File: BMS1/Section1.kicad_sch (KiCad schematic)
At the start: 68 parts

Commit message: Cap Change
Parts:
- R79: footprint Resistor_SMD:R_2512_6332Metric_Pad1.40x3.35mm_HandSolder -> Resistor_SMD:R_0603_1608Metric_Pad0.98x0.95mm_HandSolder
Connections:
- net BatteryBus.C0: now also C39.2
- net BatteryBus.C1: now also C38.2
- net BatteryBus.C10: now also C29.2
- net BatteryBus.C11: now also C28.2
- net BatteryBus.C12: now also C27.2
- net BatteryBus.C2: now also C37.2
- net BatteryBus.C3: now also C36.2
- net BatteryBus.C4: now also C35.2
- net BatteryBus.C5: now also C34.2
- net BatteryBus.C6: now also C33.2
- net BatteryBus.C7: now also C32.1
- net BatteryBus.C8: now also C31.2, C32.2; no longer C32.1
- net BatteryBus.C9: now also C30.2
- net GND1: no longer C27.2, C28.2, C29.2, C30.2, C31.2, C32.2, C33.2, C34.2, C35.2, C36.2, C37.2, C38.2, C39.2
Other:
- moved on the sheet: C27, C28, C29, C30, C31, C32, C33, C34, C35, C36, C37, C38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

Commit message: Schematic (Self) Review Done
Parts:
- C27, C28, C29, C30, C31, C32, C33, C34, C35, C36, C37, C38, C39: value 100nF -> 15u
- R67, R68, R69, R70, R71, R72, R73, R74, R75, R76, R77, R78: value 21 -> 18
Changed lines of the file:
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@@
       (effects (font (size 1.27 1.27)) (justify right))
     )
-    (property "Value" "21" (at 84.582 184.15 90)
+    (property "Value" "18" (at 84.582 184.15 90)
       (effects (font (size 1.27 1.27)) (justify right))
     )
@@
       (effects (font (size 1.27 1.27)) (justify right))
     )
-    (property "Value" "21" (at 84.963 107.95 90)
+    (property "Value" "18" (at 84.963 107.95 90)
       (effects (font (size 1.27 1.27)) (justify right))
     )
@@
       (effects (font (size 1.27 1.27)) (justify right))
     )
-    (property "Value" "21" (at 85.471 168.783 90)
+    (property "Value" "18" (at 85.471 168.783 90)
       (effects (font (size 1.27 1.27)) (justify right))
     )
@@
       (effects (font (size 1.27 1.27)) (justify right))
     )
-    (property "Value" "21" (at 85.725 214.503 90)
+    (property "Value" "18" (at 85.725 214.503 90)
       (effects (font (size 1.27 1.27)) (justify right))
     )
@@
       (effects (font (size 1.27 1.27)))
     )
-    (property "Value" "100nF" (at 102.616 99.06 0)
+    (property "Value" "15u" (at 102.616 99.06 0)
       (effects (font (size 1.27 1.27)))
     )
@@
       (effects (font (size 1.27 1.27)) (justify right))
     )
-    (property "Value" "21" (at 84.963 123.317 90)
+    (property "Value" "18" (at 84.963 123.317 90)
       (effects (font (size 1.27 1.27)) (justify right))
     )
@@
       (effects (font (size 1.27 1.27)))
     )
-    (property "Value" "100nF" (at 102.87 128.778 0)
+    (property "Value" "15u" (at 102.87 128.778 0)
       (effects (font (size 1.27 1.27)))
     )
@@
       (effects (font (size 1.27 1.27)) (justify right))
     )
-    (property "Value" "21" (at 84.836 92.964 90)
+    (property "Value" "18" (at 84.836 92.964 90)
       (effects (font (size 1.27 1.27)) (justify right))
     )
@@
       (effects (font (size 1.27 1.27)))
     )
-    (property "Value" "100nF" (at 102.616 37.592 0)
+    (property "Value" "15u" (at 102.616 37.592 0)
       (effects (font (size 1.27 1.27)))
     )
@@
       (effects (font (size 1.27 1.27)))
     )
-    (property "Value" "100nF" (at 103.124 173.99 0)
+    (property "Value" "15u" (at 103.124 173.99 0)
       (effects (font (size 1.27 1.27)))
     )
@@
       (effects (font (size 1.27 1.27)))
     )
-    (property "Value" "100nF" (at 102.87 205.232 0)
+    (property "Value" "15u" (at 102.87 205.232 0)
       (effects (font (size 1.27 1.27)))
     )
@@
       (effects (font (size 1.27 1.27)) (justify right))
     )
-    (property "Value" "21" (at 85.217 153.416 90)
+    (property "Value" "18" (at 85.217 153.416 90)
       (effects (font (size 1.27 1.27)) (justify right))
     )
@@
       (effects (font (size 1.27 1.27)) (justify right))
     )
-    (property "Value" "21" (at 85.217 46.99 90)
+    (property "Value" "18" (at 85.217 46.99 90)
       (effects (font (size 1.27 1.27)) (justify right))
     )
@@
       (effects (font (size 1.27 1.27)) (justify right))
     )
-    (property "Value" "21" (at 84.963 199.39 90)
+    (property "Value" "18" (at 84.963 199.39 90)
       (effects (font (size 1.27 1.27)) (justify right))
     )
@@
       (effects (font (size 1.27 1.27)))
     )
-    (property "Value" "100nF" (at 103.632 144.78 0)
+    (property "Value" "15u" (at 103.632 144.78 0)
       (effects (font (size 1.27 1.27)))
     )
@@
       (effects (font (size 1.27 1.27)))
     )
-    (property "Value" "100nF" (at 102.616 221.107 0)
+    (property "Value" "15u" (at 102.616 221.107 0)
       (effects (font (size 1.27 1.27)))
     )
@@
       (effects (font (size 1.27 1.27)) (justify right))
     )
-    (property "Value" "21" (at 86.995 62.103 90)
+    (property "Value" "18" (at 86.995 62.103 90)
       (effects (font (size 1.27 1.27)) (justify right))
     )
@@
       (effects (font (size 1.27 1.27)))
     )
-    (property "Value" "100nF" (at 103.378 159.766 0)
+    (property "Value" "15u" (at 103.378 159.766 0)
       (effects (font (size 1.27 1.27)))
     )
@@
       (effects (font (size 1.27 1.27)))
     )
-    (property "Value" "100nF" (at 102.616 113.03 0)
+    (property "Value" "15u" (at 102.616 113.03 0)
       (effects (font (size 1.27 1.27)))
     )
@@
       (effects (font (size 1.27 1.27)))
     )
-    (property "Value" "100nF" (at 102.362 68.326 0)
+    (property "Value" "15u" (at 102.362 68.326 0)
       (effects (font (size 1.27 1.27)))
     )
@@
       (effects (font (size 1.27 1.27)))
     )
-    (property "Value" "100nF" (at 102.362 83.312 0)
+    (property "Value" "15u" (at 102.362 83.312 0)
       (effects (font (size 1.27 1.27)))
     )
@@
       (effects (font (size 1.27 1.27)))
     )
-    (property "Value" "100nF" (at 102.616 53.086 0)
+    (property "Value" "15u" (at 102.616 53.086 0)
       (effects (font (size 1.27 1.27)))
     )
@@
       (effects (font (size 1.27 1.27)))
     )
-    (property "Value" "100nF" (at 102.87 189.484 0)
+    (property "Value" "15u" (at 102.87 189.484 0)
       (effects (font (size 1.27 1.27)))
     )
@@
       (effects (font (size 1.27 1.27)) (justify right))
     )
-    (property "Value" "21" (at 84.328 138.43 90)
+    (property "Value" "18" (at 84.328 138.43 90)
       (effects (font (size 1.27 1.27)) (justify right))
     )
@@
       (effects (font (size 1.27 1.27)) (justify right))
     )
-    (property "Value" "21" (at 85.217 77.724 90)
-      (effects (font (size 1.27 1.27)) (justify right))
-    )
+    (property "Value" "18" (at 85.217 77.724 90)
+      (effects (font (size 1.27 1.27)) (justify right))
+    )

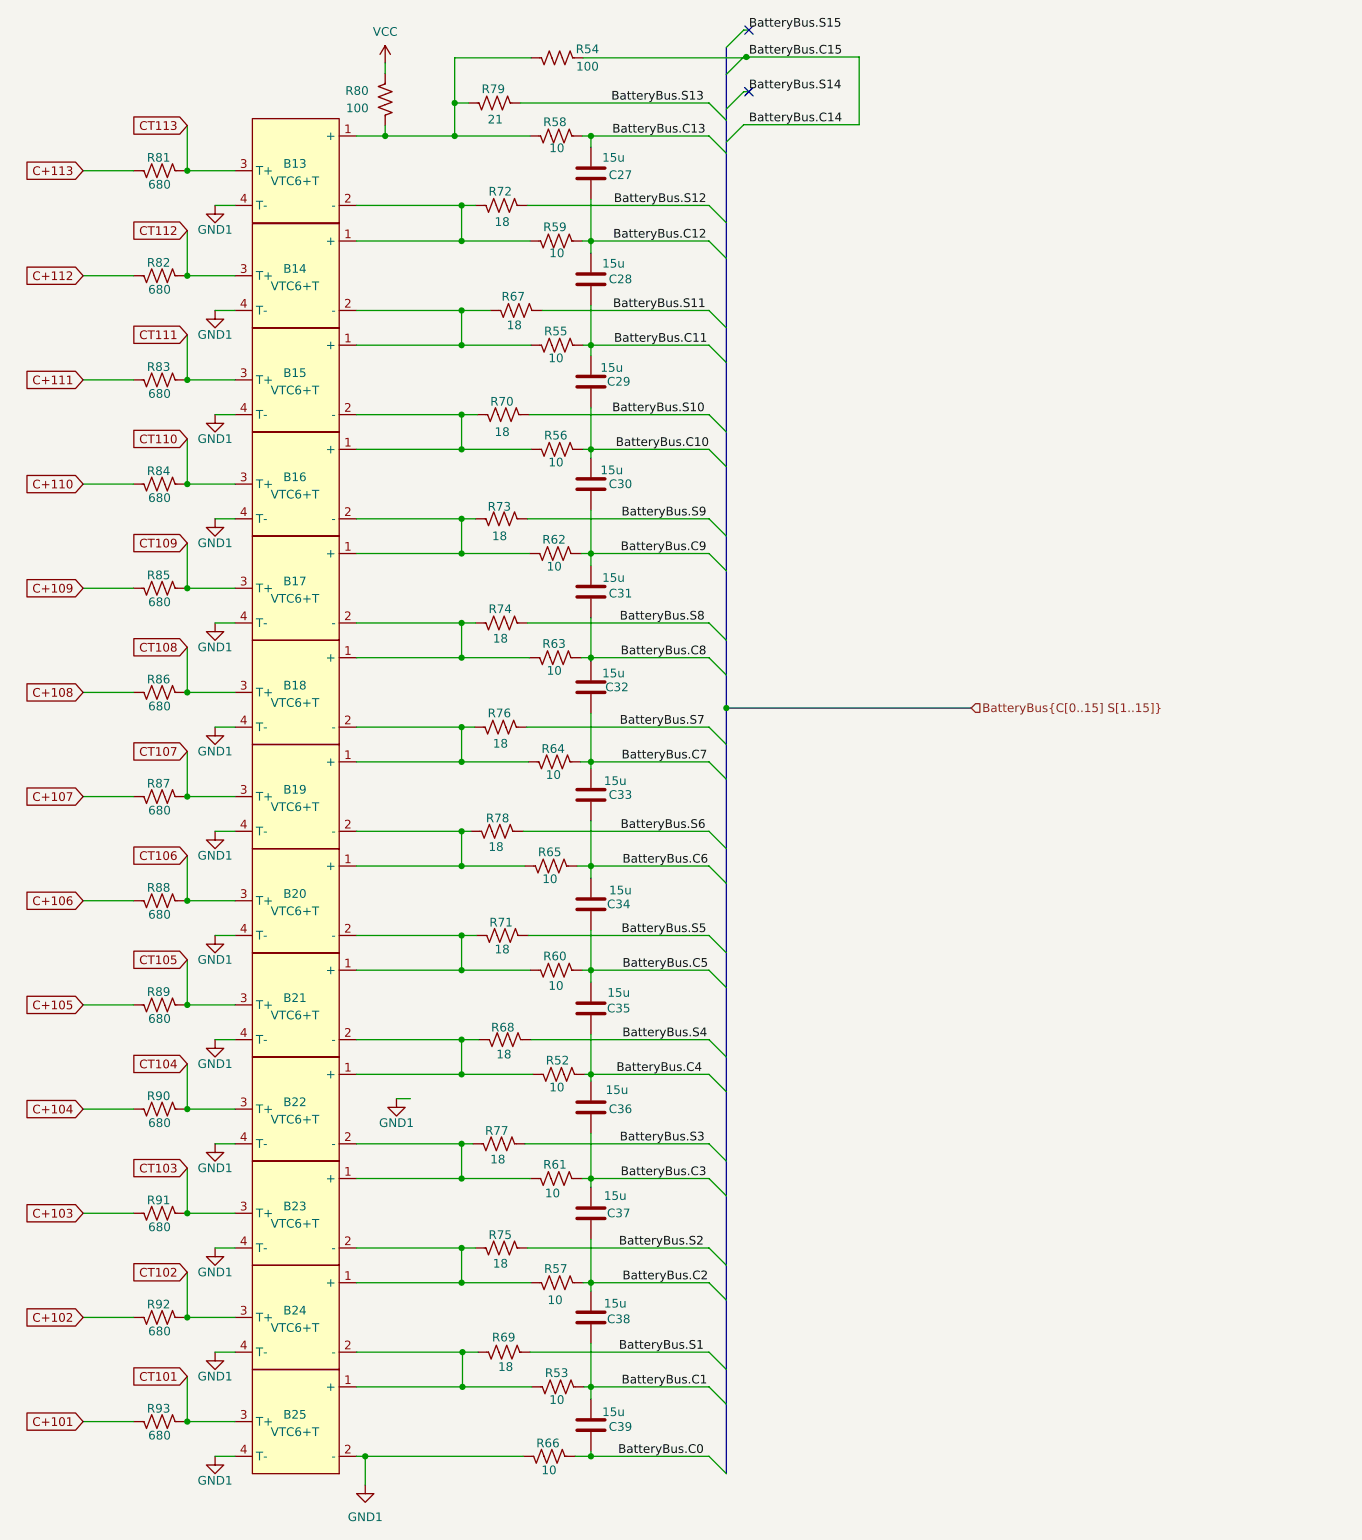
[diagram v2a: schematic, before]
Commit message: fixed to whats on board footy not changed
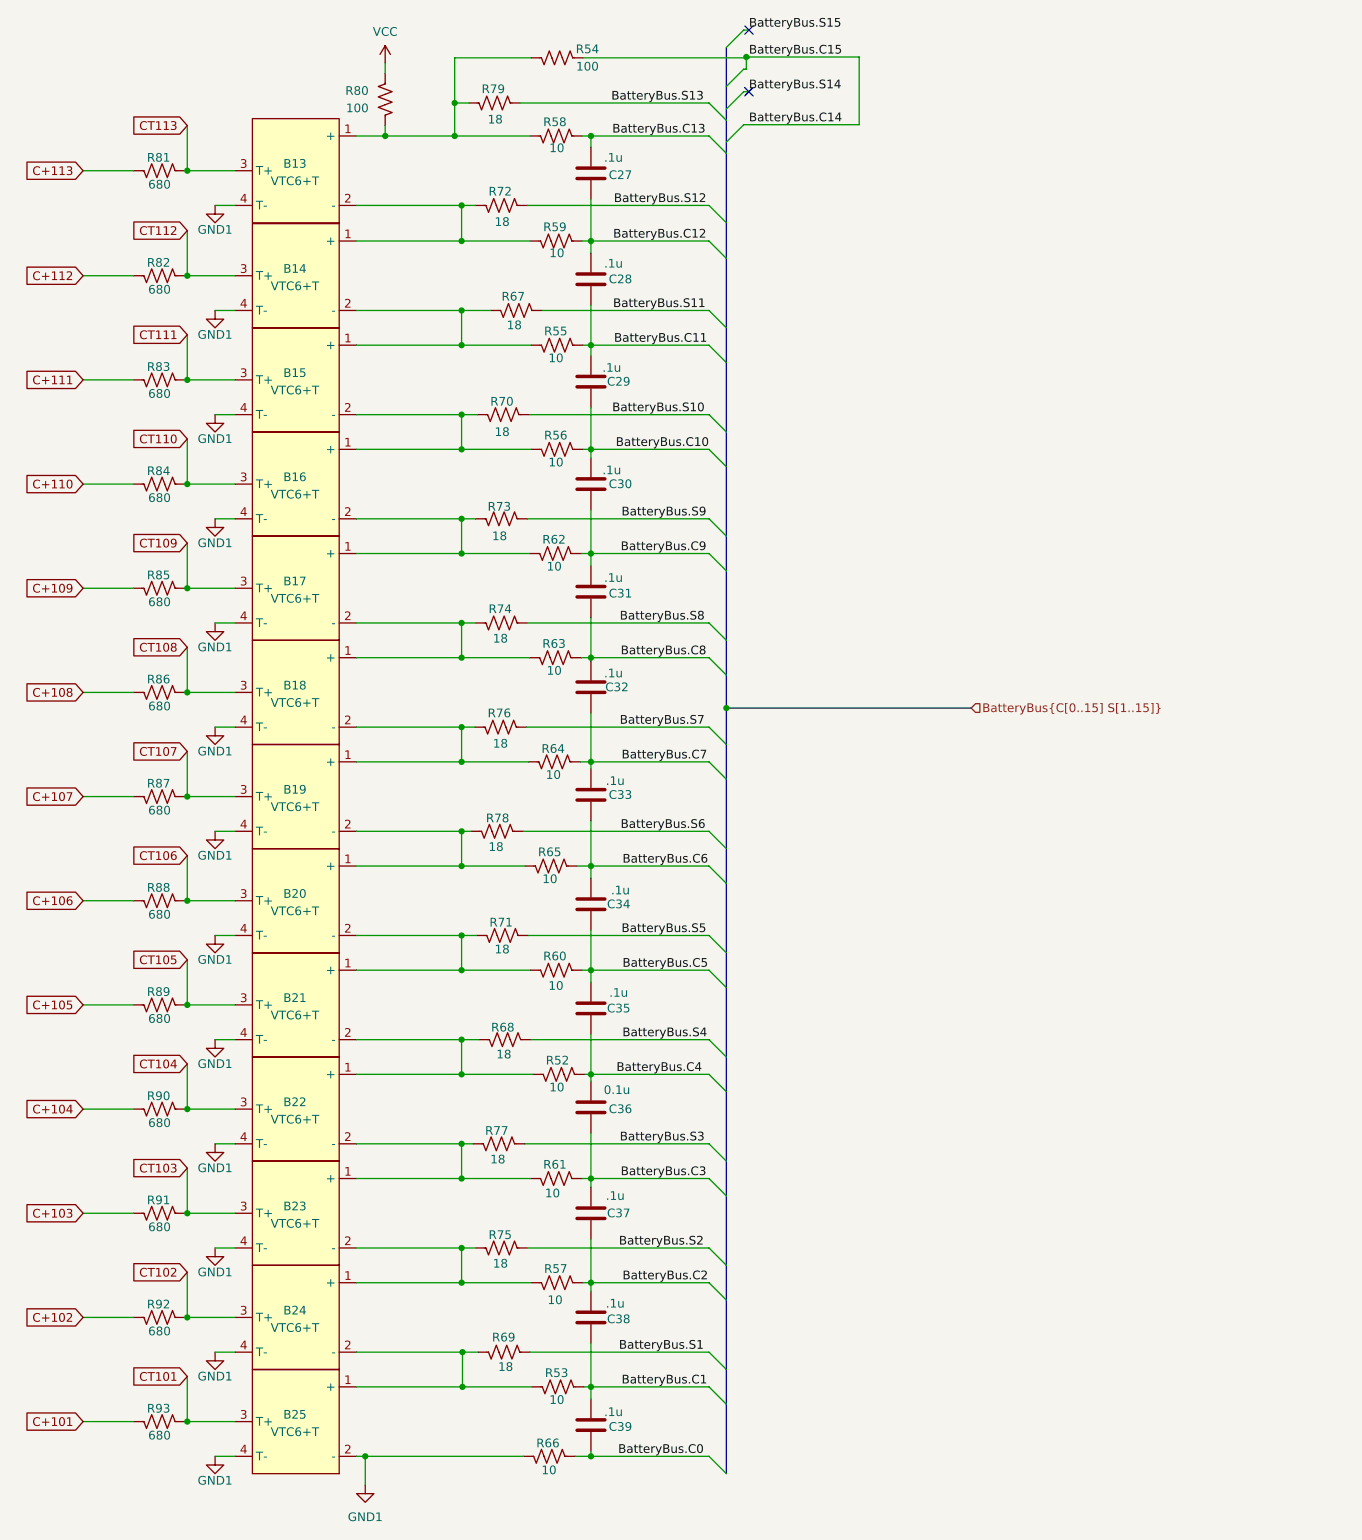
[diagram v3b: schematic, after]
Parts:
- C27, C28, C29, C30, C31, C32, C33, C34, C35, C37, C38, C39: value 15u -> .1u
- C36: value 15u -> 0.1u
- R79: value 21 -> 18
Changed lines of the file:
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@@
     (stroke (width 0) (type default))
   )
-  (bus_entry (at 119.126 25.4) (size 2.54 -2.54)
+  (bus_entry (at 119.126 27.178) (size 2.54 -2.54)
     (stroke (width 0) (type default))
   )
@@
     (stroke (width 0) (type default))
   )
-  (bus (pts (xy 119.126 25.4) (xy 119.126 30.48))
+  (bus (pts (xy 119.126 27.178) (xy 119.126 30.48))
     (stroke (width 0) (type default))
   )
@@
     (stroke (width 0) (type default))
   )
+  (wire (pts (xy 122.047 24.638) (xy 122.047 22.86))
+    (stroke (width 0) (type default))
+  )
   (bus (pts (xy 119.126 52.324) (xy 119.126 47.117))
     (stroke (width 0) (type default))
@@
     (stroke (width 0) (type default))
   )
-  (bus (pts (xy 119.126 21.463) (xy 119.126 25.4))
+  (bus (pts (xy 119.126 21.463) (xy 119.126 27.178))
     (stroke (width 0) (type default))
   )
@@
     (stroke (width 0) (type default))
   )
-  (wire (pts (xy 122.047 22.86) (xy 121.666 22.86))
+  (wire (pts (xy 122.047 24.638) (xy 121.666 24.638))
     (stroke (width 0) (type default))
   )
@@
     (stroke (width 0) (type default))
   )
-  (wire (pts (xy 70.866 175.26) (xy 72.898 175.26))
-    (stroke (width 0) (type default))
-  )
   (wire (pts (xy 80.391 197.104) (xy 65.024 197.104))
     (stroke (width 0) (type default))
@@
       (effects (font (size 1.27 1.27)))
     )
-    (property "Value" "15u" (at 102.616 99.06 0)
+    (property "Value" ".1u" (at 102.616 99.06 0)
       (effects (font (size 1.27 1.27)))
     )
@@
       (effects (font (size 1.27 1.27)) (justify right))
     )
-    (property "Value" "21" (at 84.201 32.004 90)
+    (property "Value" "18" (at 84.201 32.004 90)
       (effects (font (size 1.27 1.27)) (justify right))
     )
@@
       (effects (font (size 1.27 1.27)))
     )
-    (property "Value" "15u" (at 102.87 128.778 0)
+    (property "Value" ".1u" (at 102.87 128.778 0)
       (effects (font (size 1.27 1.27)))
     )
@@
       (effects (font (size 1.27 1.27)))
     )
-    (property "Value" "15u" (at 102.616 37.592 0)
+    (property "Value" ".1u" (at 102.616 37.592 0)
       (effects (font (size 1.27 1.27)))
     )
@@
       (effects (font (size 1.27 1.27)))
     )
-    (property "Value" "15u" (at 103.124 173.99 0)
+    (property "Value" "0.1u" (at 103.124 173.99 0)
       (effects (font (size 1.27 1.27)))
     )
@@
       (effects (font (size 1.27 1.27)))
     )
-    (property "Value" "15u" (at 102.87 205.232 0)
+    (property "Value" ".1u" (at 102.87 205.232 0)
       (effects (font (size 1.27 1.27)))
     )
@@
       (effects (font (size 1.27 1.27)))
     )
-    (property "Value" "15u" (at 103.632 144.78 0)
+    (property "Value" ".1u" (at 103.632 144.78 0)
       (effects (font (size 1.27 1.27)))
     )
@@
       (effects (font (size 1.27 1.27)))
     )
-    (property "Value" "15u" (at 102.616 221.107 0)
+    (property "Value" ".1u" (at 102.616 221.107 0)
       (effects (font (size 1.27 1.27)))
     )
@@
       (effects (font (size 1.27 1.27)))
     )
-    (property "Value" "15u" (at 103.378 159.766 0)
+    (property "Value" ".1u" (at 103.378 159.766 0)
       (effects (font (size 1.27 1.27)))
     )
@@
       (effects (font (size 1.27 1.27)))
     )
-    (property "Value" "15u" (at 102.616 113.03 0)
+    (property "Value" ".1u" (at 102.616 113.03 0)
       (effects (font (size 1.27 1.27)))
     )
@@
       (effects (font (size 1.27 1.27)))
     )
-    (property "Value" "15u" (at 102.362 68.326 0)
+    (property "Value" ".1u" (at 102.362 68.326 0)
       (effects (font (size 1.27 1.27)))
     )
@@
       (effects (font (size 1.27 1.27)))
     )
-    (property "Value" "15u" (at 102.362 83.312 0)
+    (property "Value" ".1u" (at 102.362 83.312 0)
       (effects (font (size 1.27 1.27)))
     )
@@
       (effects (font (size 1.27 1.27)))
     )
-    (property "Value" "15u" (at 102.616 53.086 0)
+    (property "Value" ".1u" (at 102.616 53.086 0)
       (effects (font (size 1.27 1.27)))
     )
@@
     )
   )
-  (symbol (lib_id "power:GND1") (at 70.866 175.26 0) (mirror y) (unit 1)
-    (in_bom yes) (on_board yes) (dnp no)
-    (property "Reference" "#PWR0130" (at 70.866 181.61 0)
-      (effects (font (size 1.27 1.27)) hide)
-    )
-    (property "Value" "GND1" (at 70.866 178.816 0)
-      (effects (font (size 1.27 1.27)))
-    )
-    (property "Footprint" "" (at 70.866 175.26 0)
-      (effects (font (size 1.27 1.27)) hide)
-    )
-    (property "Datasheet" "" (at 70.866 175.26 0)
-      (effects (font (size 1.27 1.27)) hide)
-    )
-    (pin "1")
-    (instances
-      (project "BMS1"
-        (path "/03933f33-7fdb-43de-9d7d-a565cad8a277"
-          (reference "#PWR0130") (unit 1)
-        )
-        (path "/03933f33-7fdb-43de-9d7d-a565cad8a277/3a675bcb-ccc0-4c98-bd4c-d3273b99074d"
-          (reference "#PWR072") (unit 1)
-        )
-      )
-    )
-  )
   (symbol (lib_id "Device:R_US") (at 36.195 176.784 270) (mirror x) (unit 1)
     (in_bom yes) (on_board yes) (dnp no)
@@
       (effects (font (size 1.27 1.27)))
     )
-    (property "Value" "15u" (at 102.87 189.484 0)
+    (property "Value" ".1u" (at 102.87 189.484 0)
       (effects (font (size 1.27 1.27)))
     )

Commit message: Added text
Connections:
- net at B24.1 (+), R57.1, R75.1: no longer B23.2 (-)
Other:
- note added: "Only keep + holes, delete negative wires, (except for B25) Delete squares on footprint (not little circled!) pg 86, Fig 47. Use schematic on the right"
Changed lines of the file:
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@@
   (junction (at 40.259 146.304) (diameter 0) (color 0 0 0 0)
-  )
-  (junction (at 80.391 197.104) (diameter 0) (color 0 0 0 0)
   )
   (junction (at 40.259 115.824) (diameter 0) (color 0 0 0 0)
@@
     (stroke (width 0) (type default))
   )
-  (wire (pts (xy 80.391 197.104) (xy 65.024 197.104))
-    (stroke (width 0) (type default))
-  )
   (wire (pts (xy 65.024 110.744) (xy 80.391 110.744))
     (stroke (width 0) (type default))
@@
     (stroke (width 0) (type default))
   )
+  (text "Only keep + holes, delete negative wires, (except for B25)\nDelete squares on footprint (not little circled!)\npg 86, Fig 47. Use schematic on the right"
+    (at 140.462 185.42 0)
+    (effects (font (size 1.27 1.27)) (justify left bottom))
+  )
   (label "BatteryBus.S6" (at 116.078 136.144 180) (fields_autoplaced)
